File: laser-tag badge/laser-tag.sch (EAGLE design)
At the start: 54 parts, among them J1 JUMPER_SOLDER_1X2_CLOSED, J3 JUMPER_SOLDER_1X2_CLOSED, J4 JUMPER_SOLDER_1X2_CLOSED, J5 JUMPER_SOLDER_1X2_CLOSED, P1 E1260CS021, Q1 2N7002, Q2 BSS123, Q3 BSS123, U1 MKL27Z256VLH4

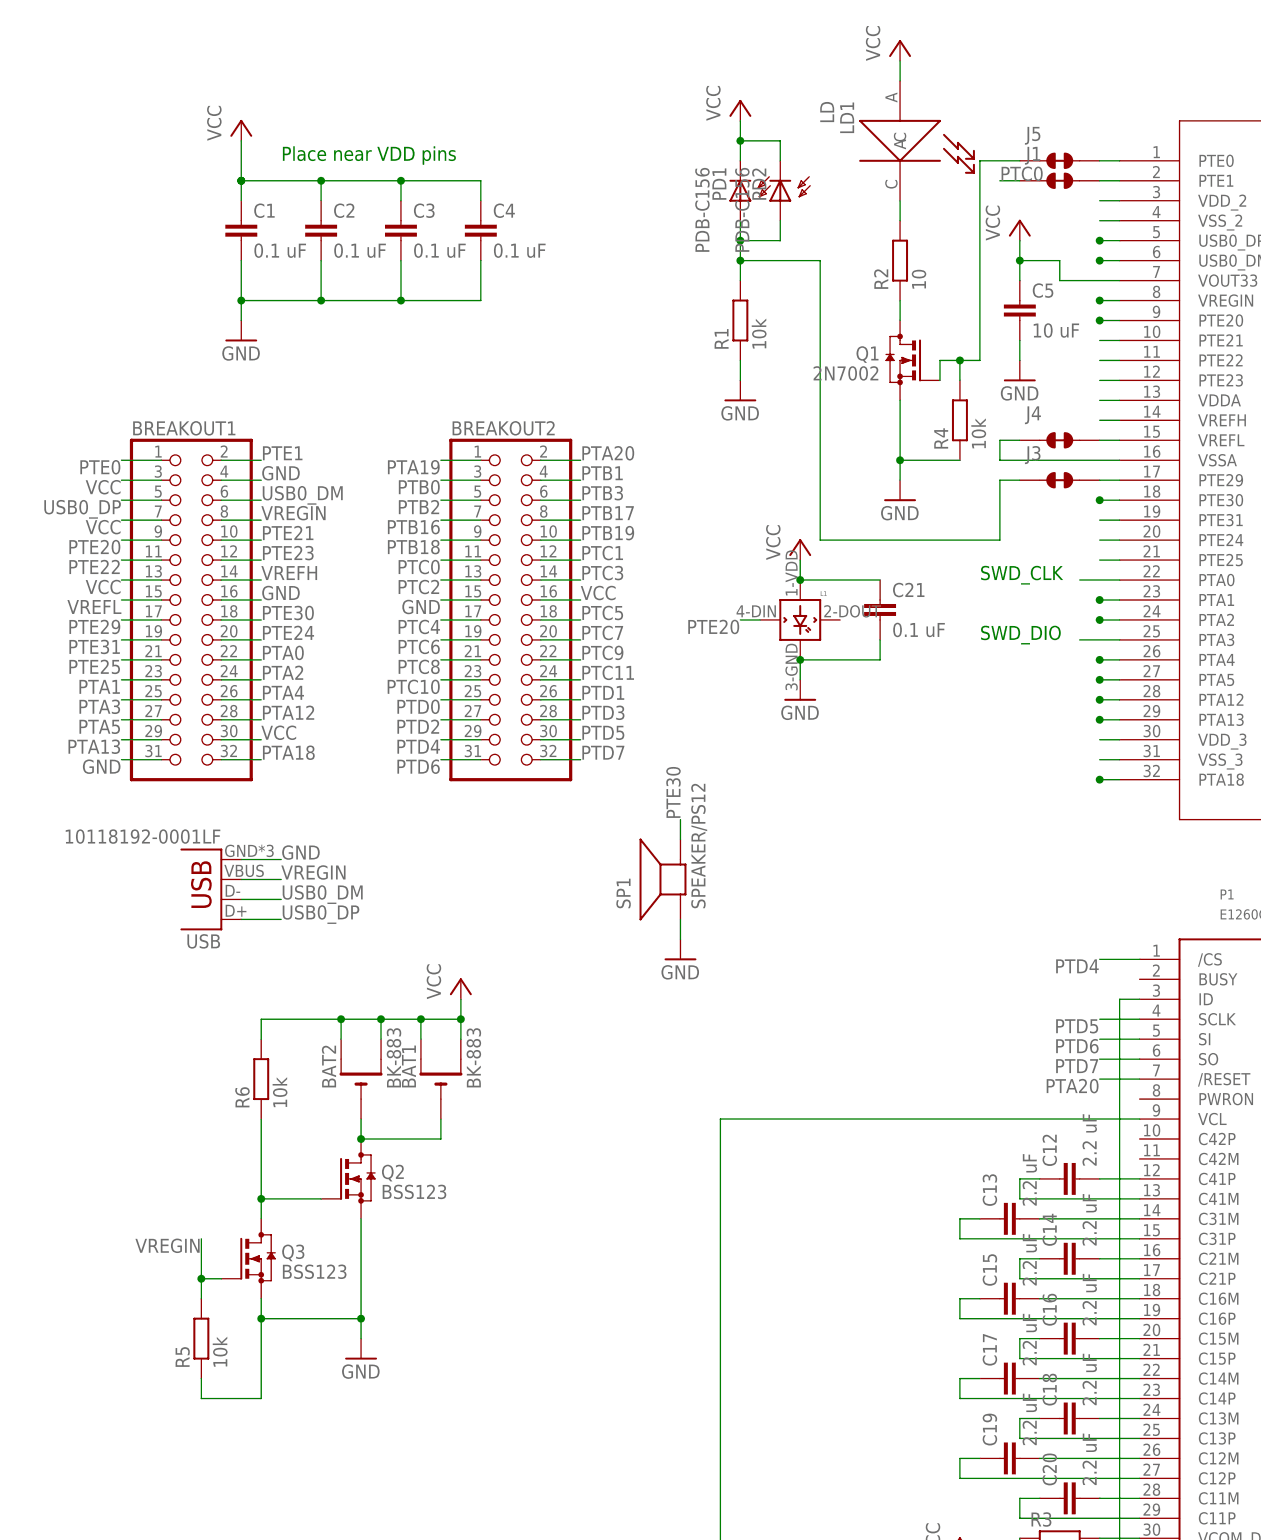
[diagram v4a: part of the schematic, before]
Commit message: Revert "Battery protection circuit"
This reverts commit 69dbc586ce164c6a939ac46ac2dad6727082318c.
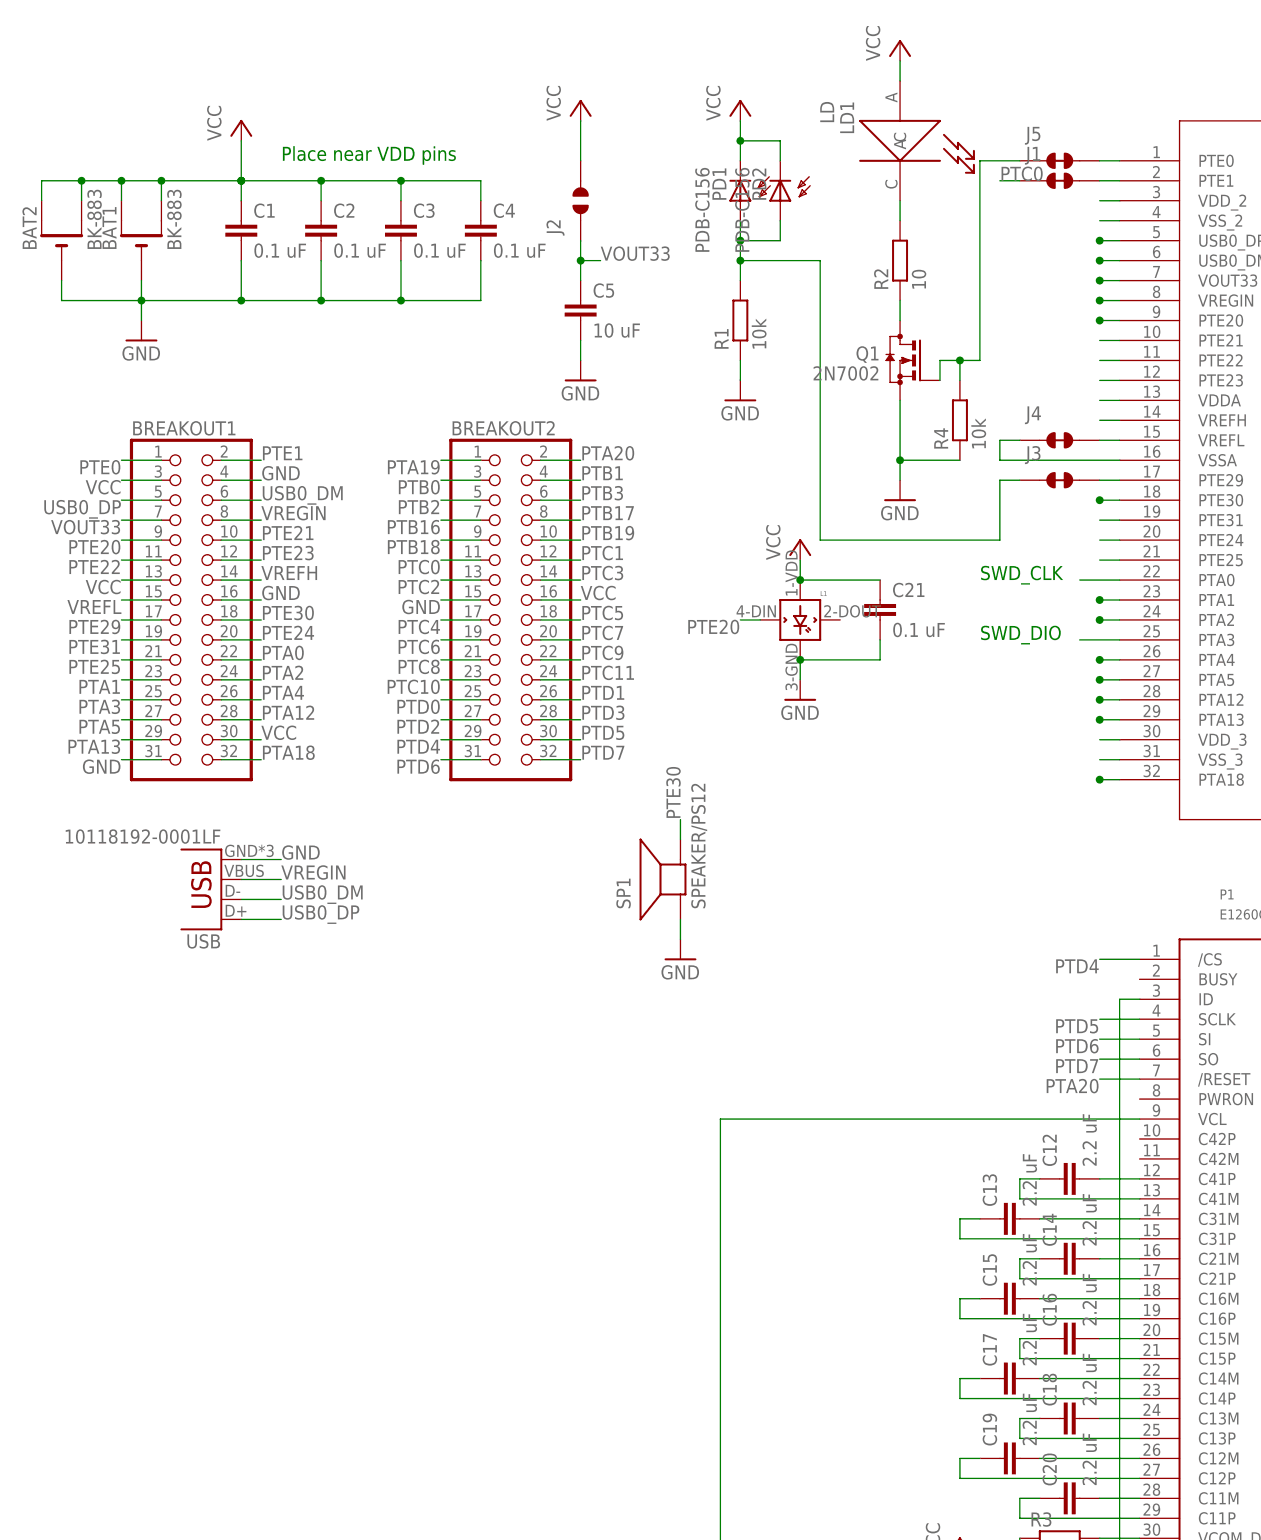
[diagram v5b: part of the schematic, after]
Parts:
- removed Q2, Q3: BSS123, transistor-small-signal:BSS123
- removed R5, R6: 10k, rcl:R-EU_R0603
- added J2: JUMPER_SOLDER_1X2_OPEN, Jumpers:JUMPER_SOLDER_1X2_OPEN
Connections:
- removed net N$31: BAT1.-, BAT2.-, Q2.D
- removed net N$32: Q2.G, Q3.D, R6.1
- new net VOUT33: BREAKOUT1.7, C5.1, J2.1, U1.VOUT33
- net GND: now also BAT1.-, BAT2.-; no longer Q2.S, Q3.S, R5.1
- net VCC: now also J2.2; no longer BREAKOUT1.7, C5.1, R6.2, U1.VOUT33
- net VREGIN: no longer Q3.G, R5.2
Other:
- moved on the sheet: BAT1, BAT2, C5

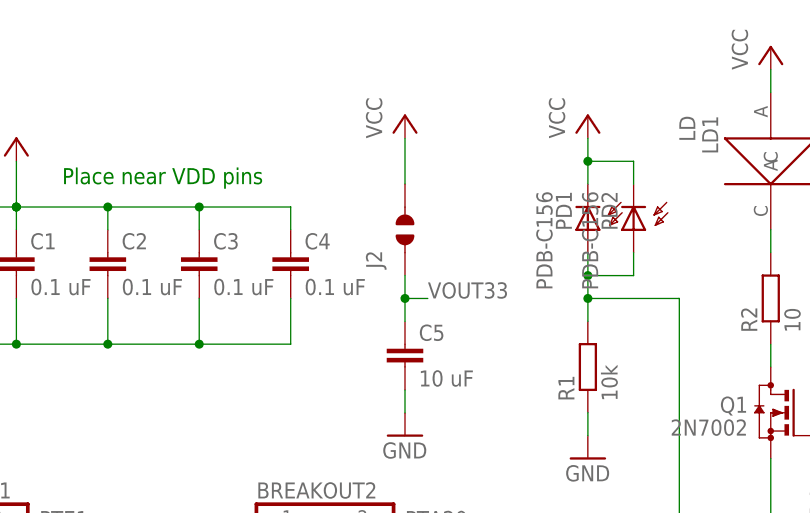
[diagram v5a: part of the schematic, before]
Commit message: Change J2 to closed
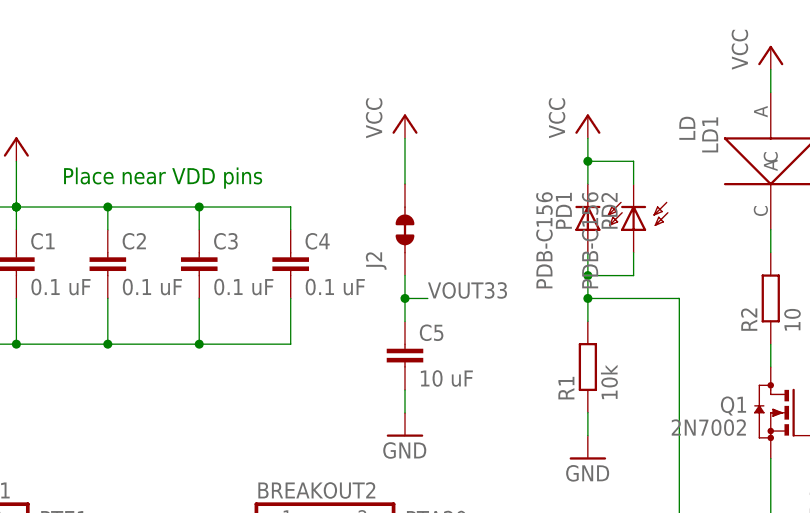
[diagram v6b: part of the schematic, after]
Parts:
- J2: value JUMPER_SOLDER_1X2_OPEN -> JUMPER_SOLDER_1X2_CLOSED; device Jumpers:JUMPER_SOLDER_1X2_OPEN -> Jumpers:JUMPER_SOLDER_1X2_CLOSED
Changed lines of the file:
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@@
 <part name="J1" library="Jumpers" deviceset="JUMPER_SOLDER_1X2_CLOSED" device=""/>
 <part name="J3" library="Jumpers" deviceset="JUMPER_SOLDER_1X2_CLOSED" device=""/>
-<part name="J2" library="Jumpers" deviceset="JUMPER_SOLDER_1X2_OPEN" device=""/>
+<part name="J2" library="Jumpers" deviceset="JUMPER_SOLDER_1X2_CLOSED" device=""/>
 <part name="PD1" library="Photonics" deviceset="PDB-C156" device=""/>
 <part name="PD2" library="Photonics" deviceset="PDB-C156" device=""/>

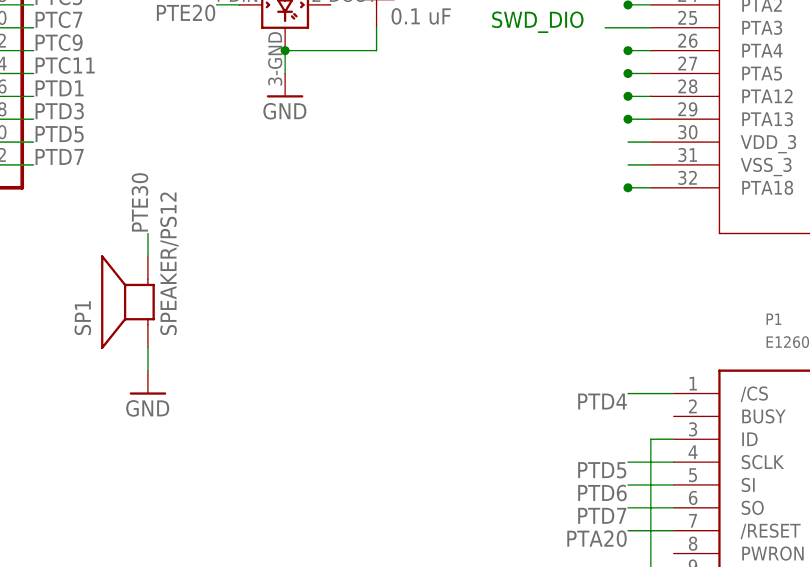
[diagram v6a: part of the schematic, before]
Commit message: Add reset button
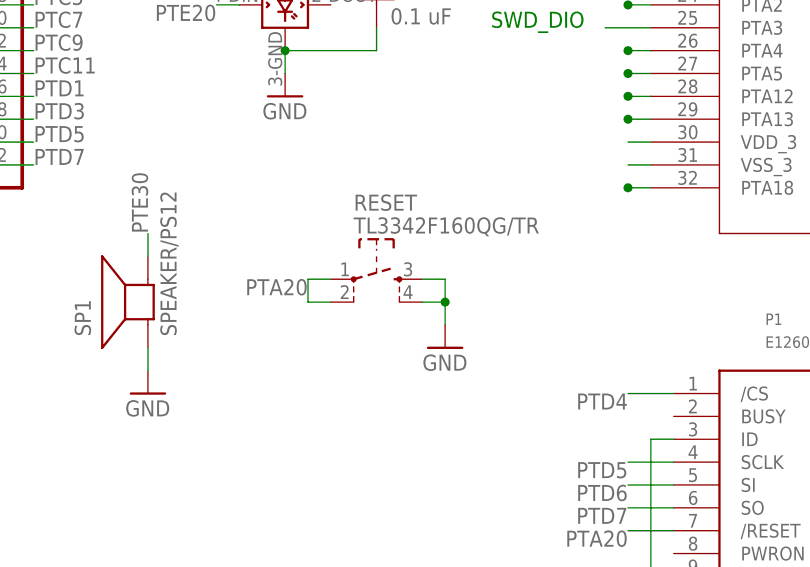
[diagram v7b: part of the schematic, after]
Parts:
- added RESET: TL3342F160QG/TR, dp_devices.v6:SW_TACT_4P
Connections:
- net GND: now also RESET.3, RESET.4
- net PTA20: now also RESET.1, RESET.2
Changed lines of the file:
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@@
 <part name="U$4" library="adafruit" deviceset="FIDUCIAL" device=""/>
 <part name="Q1" library="transistor-small-signal" deviceset="BSS123" device="" value="2N7002"/>
+<part name="RESET" library="dp_devices.v6" deviceset="SW_TACT_4P" device="" value="TL3342F160QG/TR"/>
+<part name="GND4" library="supply1" deviceset="GND" device=""/>
 </parts>
 <sheets>
@@
 <instance part="U$4" gate="G$1" x="134.62" y="-10.16"/>
 <instance part="Q1" gate="G$1" x="-17.78" y="73.66" rot="MR0"/>
+<instance part="RESET" gate="G$1" x="-20.32" y="10.16"/>
+<instance part="GND4" gate="1" x="-12.7" y="2.54"/>
 </instances>
 <busses>
@@
 <wire x1="-45.72" y1="0" x2="-45.72" y2="2.54" width="0.1524" layer="91"/>
 </segment>
+<segment>
+<pinref part="RESET" gate="G$1" pin="3"/>
+<pinref part="GND4" gate="1" pin="GND"/>
+<wire x1="-15.24" y1="10.16" x2="-12.7" y2="10.16" width="0.1524" layer="91"/>
+<wire x1="-12.7" y1="10.16" x2="-12.7" y2="7.62" width="0.1524" layer="91"/>
+<pinref part="RESET" gate="G$1" pin="4"/>
+<wire x1="-12.7" y1="7.62" x2="-12.7" y2="5.08" width="0.1524" layer="91"/>
+<wire x1="-15.24" y1="7.62" x2="-12.7" y2="7.62" width="0.1524" layer="91"/>
+<junction x="-12.7" y="7.62"/>
+</segment>
 </net>
 <net name="VCC" class="0">
@@
 <label x="7.62" y="-17.78" size="1.778" layer="95" rot="R180"/>
 </segment>
+<segment>
+<pinref part="RESET" gate="G$1" pin="2"/>
+<wire x1="-25.4" y1="7.62" x2="-27.94" y2="7.62" width="0.1524" layer="91"/>
+<wire x1="-27.94" y1="7.62" x2="-27.94" y2="10.16" width="0.1524" layer="91"/>
+<pinref part="RESET" gate="G$1" pin="1"/>
+<wire x1="-27.94" y1="10.16" x2="-25.4" y2="10.16" width="0.1524" layer="91"/>
+<label x="-27.94" y="10.16" size="1.778" layer="95" rot="R180"/>
+</segment>
 </net>

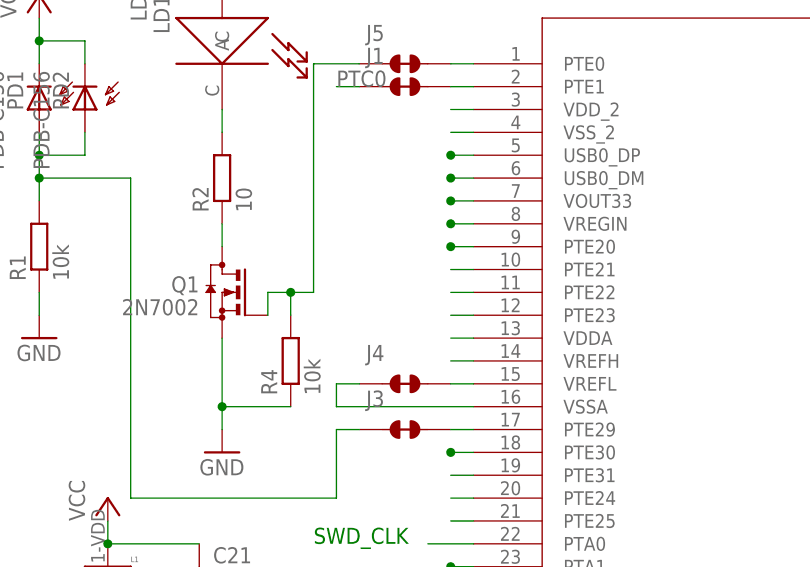
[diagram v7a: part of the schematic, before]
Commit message: Add bypass cap on VREGIN
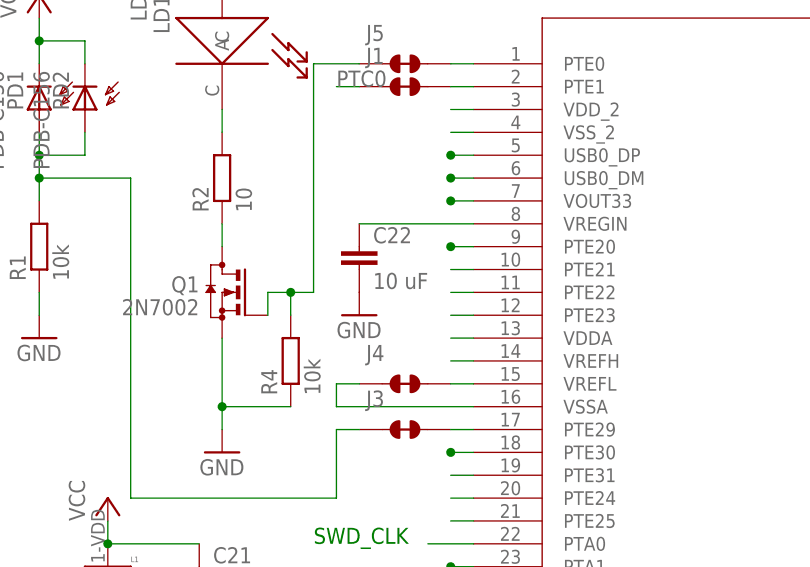
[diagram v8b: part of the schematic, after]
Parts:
- added C22: 10 uF, rcl:C-EUC0603K
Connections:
- net GND: now also C22.2
- net VREGIN: now also C22.1
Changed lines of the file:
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@@
 <part name="RESET" library="dp_devices.v6" deviceset="SW_TACT_4P" device="" value="TL3342F160QG/TR"/>
 <part name="GND4" library="supply1" deviceset="GND" device=""/>
+<part name="C22" library="rcl" deviceset="C-EU" device="C0603K" value="10 uF"/>
+<part name="GND10" library="supply1" deviceset="GND" device=""/>
 </parts>
 <sheets>
@@
 <instance part="RESET" gate="G$1" x="-20.32" y="10.16"/>
 <instance part="GND4" gate="1" x="-12.7" y="2.54"/>
+<instance part="C22" gate="G$1" x="-2.54" y="78.74"/>
+<instance part="GND10" gate="1" x="-2.54" y="71.12"/>
 </instances>
 <busses>
@@
 <junction x="-12.7" y="7.62"/>
 </segment>
+<segment>
+<pinref part="C22" gate="G$1" pin="2"/>
+<pinref part="GND10" gate="1" pin="GND"/>
+</segment>
 </net>
 <net name="VCC" class="0">
@@
 <segment>
 <pinref part="U1" gate="A" pin="VREGIN"/>
-<wire x1="10.16" y1="81.28" x2="7.62" y2="81.28" width="0.1524" layer="91"/>
-<junction x="7.62" y="81.28"/>
-</segment>
-<segment>
+<pinref part="C22" gate="G$1" pin="1"/>
+<wire x1="10.16" y1="81.28" x2="-2.54" y2="81.28" width="0.1524" layer="91"/>
+</segment>
+<segment>
